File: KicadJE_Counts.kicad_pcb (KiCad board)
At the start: 2 copper layers, 242 x 128 mm, 214 parts, among them J101 In7, J102 In6, J103 In3, J104 Out10, J105 Out11, J106 Out9, J107 Out6, J201 ClockOut, J202 ClockIn, J203 Out0, J204 Out1, J205 Out2, J206 Out3, J207 Out4, J208 Out5, J209 Out6, J210 Out7, J211 Out8, J212 Out9, J213 Reset, J214 Hold, J301 Doepfer connector, J302 In_1, J303 In 2, J304 Out 1, J305 Out 2, J306 Out 1 Final, J307 Out 2 Final, P201 HEADER_2x5_Doepfer, SW201 Run, U201 LM555, U202 4017, U301 TL072, U302 TL072

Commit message: Update KicadJE_Counts.kicad_pcb
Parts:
- moved RV301 111.4 mm to (52.5, 67.5)
- moved RV303 103.2 mm to (87.5, 62.5), turned to 180 degrees
- moved RV304 102.3 mm to (87.5, 82.5), turned to 180 degrees
- moved RV302 75.9 mm to (52.8, 87.5)
- moved J303 70.4 mm to (80.0, 115.0), turned to 90 degrees
- moved D311 54.1 mm to (86.5, 145.0), turned to 270 degrees
- moved C312 51.7 mm to (86.7, 173.8)
- moved R306 51.7 mm to (91.4, 174.2)
- moved R314 51.7 mm to (97.2, 174.6)
- moved D302 51.7 mm to (90.4, 236.3)
- moved D309 51.7 mm to (90.7, 239.6)
- moved J304 51.5 mm to (60.0, 135.0), turned to 270 degrees
- moved J302 51.5 mm to (60.0, 115.0), turned to 270 degrees
- moved C311 50.7 mm to (92.2, 178.2)
- moved C322 50.7 mm to (87.4, 178.2)
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
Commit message: Update KicadJE_Counts.kicad_pcb
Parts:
- added D317: LED, AJ:LED_0805_2012Metric_Pad1.15x1.40mm_HandSolder, F.Cu at (69.9, 51.0)
- added R334: 10k, AJ:R_0805_AJ, F.Cu at (65.5, 51.0)
- moved J301 0.50 mm to (68.8, 53.2)
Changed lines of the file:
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@@
     (tracks 486)
     (zones 0)
-    (modules 214)
-    (nets 101)
+    (modules 216)
+    (nets 102)
   )
   (page A4)
@@
   (net 99 /KicadJE_Counts2/POT3_H)
   (net 100 /KicadJE_Counts2/POT4_H)
+  (net 101 "Net-(D317-Pad1)")
   (net_class Default "This is the default net class."
     (clearance 0.15)
@@
     (add_net "Net-(D311-Pad2)")
     (add_net "Net-(D312-Pad2)")
+    (add_net "Net-(D317-Pad1)")
     (add_net "Net-(J101-PadT)")
     (add_net "Net-(J102-PadT)")
@@
   )
   (module Connector_PinSocket_2.54mm:PinSocket_2x08_P2.54mm_Vertical (layer B.Cu)
-    (at 68.71 52.75 180)
+    (at 68.75 53.25 180)
     (descr "Through hole straight socket strip, 2x08, 2.54mm pitch, double cols (from Kicad 4.0.7), script generated")
     (tags "Through hole socket strip THT 2x08 2.54mm double row")
@@
       (at (xyz 0 0 0))
       (scale (xyz 1 1 1))
+      (rotate (xyz 0 0 0))
+    )
+  )
+  (module AJ:LED_0805_2012Metric_Pad1.15x1.40mm_HandSolder (layer F.Cu)
+    (at 69.920001 51.020001)
+    (descr "LED SMD 0805 (2012 Metric), square (rectangular) end terminal, IPC_7351 nominal, (Body size source: https://docs.google.com/spreadsheets/d/1BsfQQcO9C6DZCsRaXUlFlo91Tg2WpOkGARC1WS5S8t0/edit?usp=sharing), generated with kicad-footprint-generator")
+    (tags "LED handsolder")
+    (attr smd)
+    (fp_text reference D317 (at 4.079999 -0.020001) (layer F.SilkS)
+      (effects (font (size 1 1) (thickness 0.15)))
+    )
+    (fp_text value LED (at 4.829999 1.479999) (layer F.SilkS)
+      (effects (font (size 1 1) (thickness 0.1)))
+    )
+    (fp_text user %R (at 0 0) (layer F.Fab)
+      (effects (font (size 0.5 0.5) (thickness 0.08)))
+    )
+    (fp_line (start 1.85 0.95) (end -1.85 0.95) (layer F.CrtYd) (width 0.05))
+    (fp_line (start 1.85 -0.95) (end 1.85 0.95) (layer F.CrtYd) (width 0.05))
+    (fp_line (start -1.85 -0.95) (end 1.85 -0.95) (layer F.CrtYd) (width 0.05))
+    (fp_line (start -1.85 0.95) (end -1.85 -0.95) (layer F.CrtYd) (width 0.05))
+    (fp_line (start -1.86 0.96) (end 1 0.96) (layer F.SilkS) (width 0.12))
+    (fp_line (start -1.86 -0.96) (end -1.86 0.96) (layer F.SilkS) (width 0.12))
+    (fp_line (start 1 -0.96) (end -1.86 -0.96) (layer F.SilkS) (width 0.12))
+    (fp_line (start 1 0.6) (end 1 -0.6) (layer F.Fab) (width 0.1))
+    (fp_line (start -1 0.6) (end 1 0.6) (layer F.Fab) (width 0.1))
+    (fp_line (start -1 -0.3) (end -1 0.6) (layer F.Fab) (width 0.1))
+    (fp_line (start -0.7 -0.6) (end -1 -0.3) (layer F.Fab) (width 0.1))
+    (fp_line (start 1 -0.6) (end -0.7 -0.6) (layer F.Fab) (width 0.1))
+    (pad 2 smd roundrect (at 1.025 0) (size 1.15 1.4) (layers F.Cu F.Paste F.Mask) (roundrect_rratio 0.217391)
+      (net 1 GND))
+    (pad 1 smd roundrect (at -1.025 0) (size 1.15 1.4) (layers F.Cu F.Paste F.Mask) (roundrect_rratio 0.217391)
+      (net 101 "Net-(D317-Pad1)"))
+    (model ${KISYS3DMOD}/LED_SMD.3dshapes/LED_0805_2012Metric.wrl
+      (at (xyz 0 0 0))
+      (scale (xyz 1 1 1))
+      (rotate (xyz 0 0 0))
+    )
+  )
+  (module AJ:R_0805_AJ (layer F.Cu)
+    (at 65.5 51)
+    (descr "Resistor SMD 0805 (2012 Metric), square (rectangular) end terminal, IPC_7351 nominal with elongated pad for handsoldering. (Body size source: https://docs.google.com/spreadsheets/d/1BsfQQcO9C6DZCsRaXUlFlo91Tg2WpOkGARC1WS5S8t0/edit?usp=sharing), generated with kicad-footprint-generator")
+    (tags "resistor handsolder")
+    (attr smd)
+    (fp_text reference R334 (at -4 0.024999) (layer F.SilkS)
+      (effects (font (size 1 1) (thickness 0.15)))
+    )
+    (fp_text value 10k (at 0 1.65) (layer F.SilkS)
+      (effects (font (size 0.8 0.8) (thickness 0.1)))
+    )
+    (fp_line (start -1 0.6) (end -1 -0.6) (layer F.Fab) (width 0.1))
+    (fp_line (start -1 -0.6) (end 1 -0.6) (layer F.Fab) (width 0.1))
+    (fp_line (start 1 -0.6) (end 1 0.6) (layer F.Fab) (width 0.1))
+    (fp_line (start 1 0.6) (end -1 0.6) (layer F.Fab) (width 0.1))
+    (fp_line (start -0.261252 -0.71) (end 0.261252 -0.71) (layer F.SilkS) (width 0.12))
+    (fp_line (start -0.261252 0.71) (end 0.261252 0.71) (layer F.SilkS) (width 0.12))
+    (fp_line (start -1.85 0.95) (end -1.85 -0.95) (layer F.CrtYd) (width 0.05))
+    (fp_line (start -1.85 -0.95) (end 1.85 -0.95) (layer F.CrtYd) (width 0.05))
+    (fp_line (start 1.85 -0.95) (end 1.85 0.95) (layer F.CrtYd) (width 0.05))
+    (fp_line (start 1.85 0.95) (end -1.85 0.95) (layer F.CrtYd) (width 0.05))
+    (fp_text user %R (at 0 0) (layer F.Fab)
+      (effects (font (size 0.5 0.5) (thickness 0.08)))
+    )
+    (pad 1 smd roundrect (at -1.025 0) (size 1.15 1.4) (layers F.Cu F.Paste F.Mask) (roundrect_rratio 0.217391)
+      (net 18 -12V))
+    (pad 2 smd roundrect (at 1.025 0) (size 1.15 1.4) (layers F.Cu F.Paste F.Mask) (roundrect_rratio 0.217391)
+      (net 101 "Net-(D317-Pad1)"))
+    (model ${KISYS3DMOD}/Resistor_SMD.3dshapes/R_0805_2012Metric.wrl
+      (at (xyz 0 0 0))
+      (scale (xyz 1 1 1))

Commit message: Update KicadJE_Counts.kicad_pcb
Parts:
- C305, C306: moved to F.Cu
- RV301: value 100k_A4 -> 100k_1.1
- RV302: value 100k_A4 -> 100k_1.2
- RV303: value 100k_A4 -> 100k_2.1
- RV304: value 100k_A4 -> 100k_2.2
- moved C305 160.6 mm to (74.0, 56.4), turned to 90 degrees
- moved C306 155.3 mm to (65.8, 56.2), turned to 270 degrees
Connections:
- R328 pad 1: (no net) -> /KicadJE_Counts2/POT2_C
- RV301 pad 1: (no net) -> /KicadJE_Counts2/POT1_L
- RV301 pad 2: /KicadJE_Counts2/POT3_C -> /KicadJE_Counts2/POT1_C
- RV301 pad 3: /KicadJE_Counts2/POT3_H -> (no net)
- RV302 pad 1: /KicadJE_Counts2/POT4_L -> /KicadJE_Counts2/POT2_L
- RV302 pad 2: /KicadJE_Counts2/POT4_C -> /KicadJE_Counts2/POT2_C
- RV302 pad 3: /KicadJE_Counts2/POT4_H -> (no net)
- RV303 pad 3: /KicadJE_Counts2/POT3_H -> (no net)
- RV304 pad 3: /KicadJE_Counts2/POT4_H -> (no net)

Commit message: Update KicadJE_Counts.kicad_pcb
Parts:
- added H301: ON, AJ:LED_Hole_3mm, F.Cu at (102.0, 52.0)
- added TP301: In1, AJ:Jack_6m3, F.Cu at (102.0, 115.0)
- added TP302: Tri, AJ:Jack_6m3, F.Cu at (102.0, 135.0)
- added TP303: SQ, AJ:Jack_6m3, F.Cu at (102.0, 145.0)
- added TP304: PWM1, AJ:Pot_6m3_scale1, F.Cu at (102.0, 65.0)
- added TP305: PWM2, AJ:Pot_6m3_scale1, F.Cu at (102.0, 85.0)
- D301, D302: moved to F.Cu
- moved D302 182.8 mm to (60.0, 56.0), turned to 270 degrees
- moved D301 164.5 mm to (80.0, 56.0), turned to 90 degrees
- moved U302 130.0 mm to (60.0, 100.0), turned to 180 degrees
- moved U301 125.4 mm to (80.0, 100.0), turned to 180 degrees
- moved C309 103.4 mm to (60.0, 96.0), turned to 180 degrees
- moved C314 100.9 mm to (72.0, 115.0), turned to 180 degrees
- moved C310 100.4 mm to (60.0, 105.0)
- moved C313 97.3 mm to (68.0, 115.0)
- moved C311 83.1 mm to (80.0, 96.0), turned to 180 degrees
- moved D304 77.1 mm to (129.4, 192.7)
- moved D309 77.1 mm to (133.7, 175.6)
- moved D306 77.1 mm to (129.8, 187.5)
- moved D307 77.1 mm to (119.8, 186.5)
- moved D308 77.1 mm to (119.7, 175.4)
- moved D310 77.1 mm to (119.7, 172.1)
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
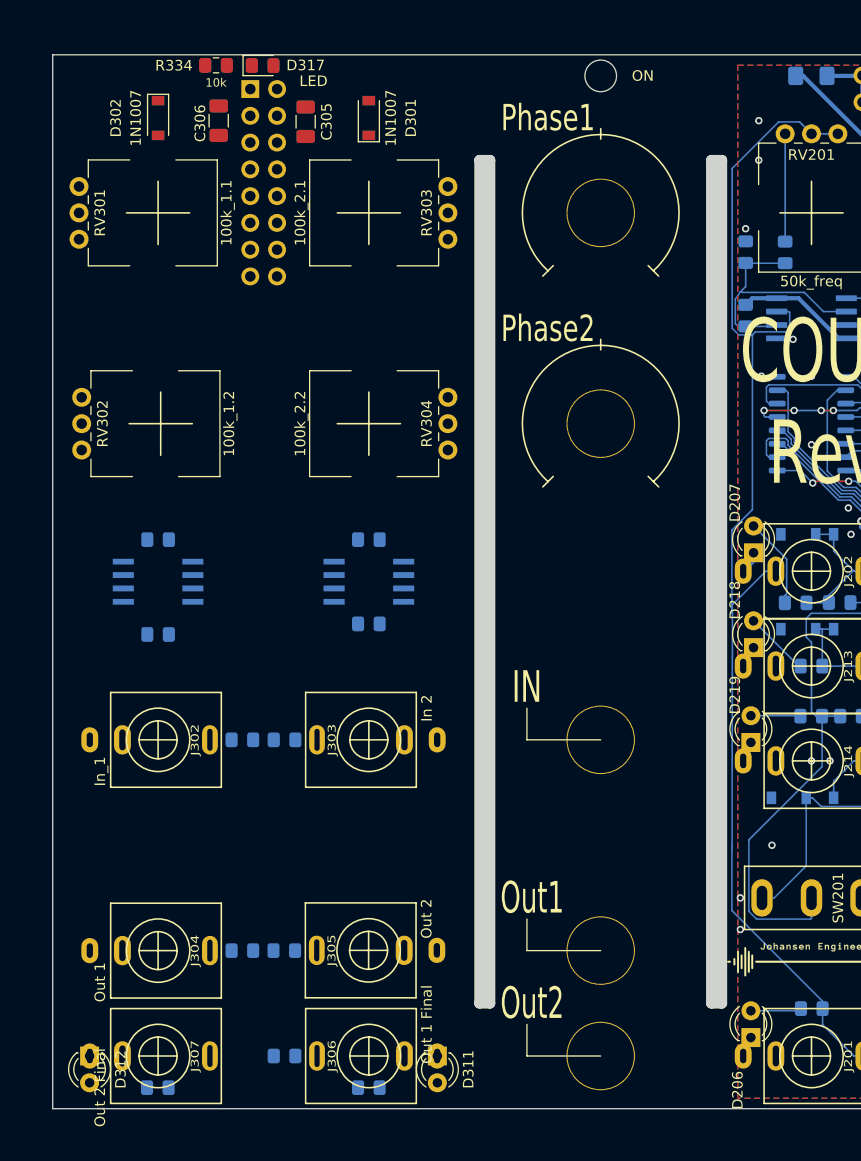
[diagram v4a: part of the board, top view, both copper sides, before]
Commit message: Update KicadJE_Counts.kicad_pcb
LED and GND on center panel
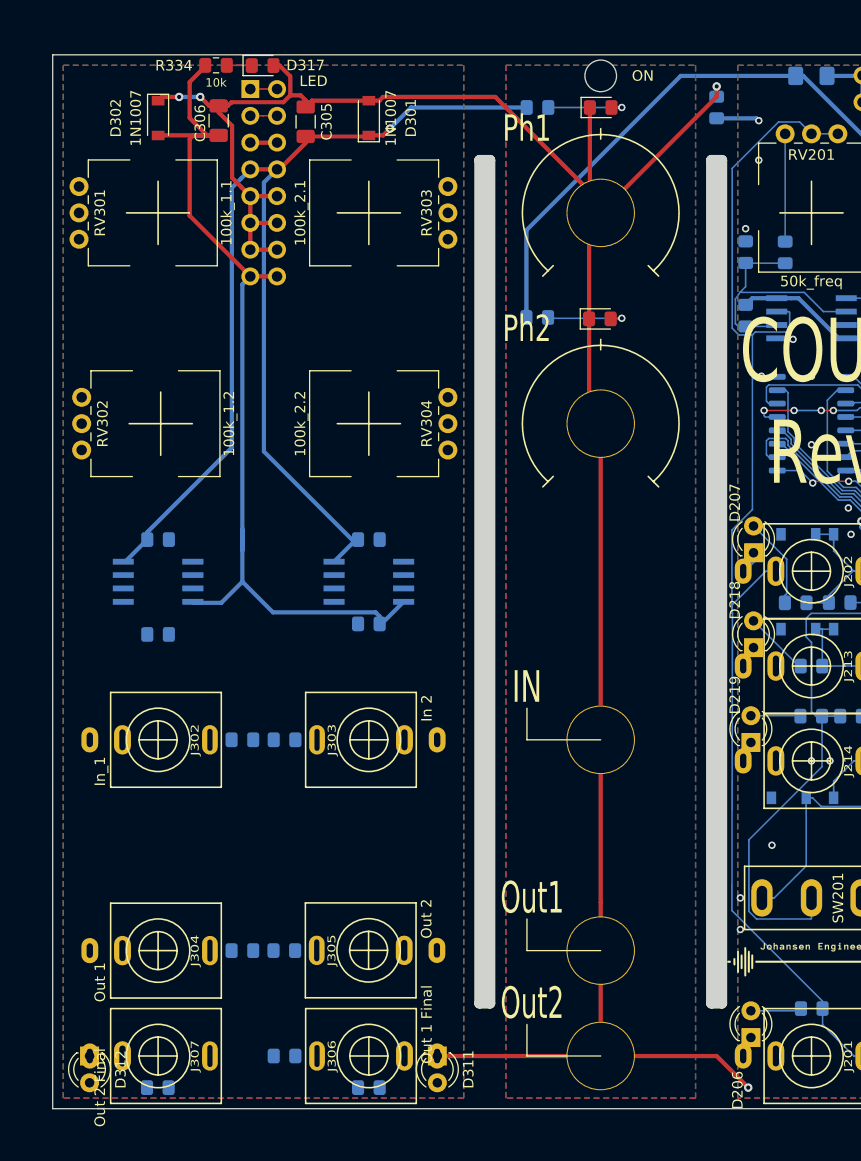
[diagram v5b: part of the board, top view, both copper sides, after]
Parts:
- added D101: D_LED, AJ:LED_0805_2012Metric_Pad1.15x1.40mm_HandSolder, F.Cu at (102.0, 55.0)
- added D102: D_LED, AJ:LED_0805_2012Metric_Pad1.15x1.40mm_HandSolder, F.Cu at (101.9, 75.1)
- added R107: DNP, AJ:R_0805_AJ, B.Cu at (96.0, 55.0)
- added R108: DNP, AJ:R_0805_AJ, B.Cu at (96.0, 74.9)
- added R109: DNP, AJ:R_0805_AJ, B.Cu at (113.0, 55.0)
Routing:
- net GND: track 0.00 -> 215.2 mm, vias 0 -> 4
- net +12V: track 0.00 -> 114.2 mm, vias 0 -> 1
- net -12V: track 0.00 -> 90.7 mm
- net +12Vc: track 94.1 -> 133.9 mm
- net Net-(D102-Pad2): track 0.00 -> 8.11 mm, vias 0 -> 1
- net Net-(D101-Pad2): track 0.00 -> 7.95 mm, vias 0 -> 1
- net GNDS: track 59.6 -> 63.7 mm
- net /KicadJE_Counts2/Gate: track 0.00 -> 2.54 mm
- net /KicadJE_Counts2/CV: track 0.00 -> 2.54 mm
- net +5V: track 0.00 -> 2.54 mm
- net Net-(D317-Pad1): track 0.00 -> 2.38 mm
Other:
- board text added: "Ph1"
- board text added: "Ph2"

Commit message: Update KicadJE_Counts.kicad_pcb
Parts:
- moved R109 3.00 mm to (110.0, 55.0)
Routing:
- net GND: track 215.2 -> 198.7 mm
- net GNDS: track 63.7 -> 66.7 mm
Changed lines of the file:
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@@
     (thickness 1.6)
     (drawings 219)
-    (tracks 607)
+    (tracks 606)
     (zones 0)
     (modules 227)
@@
   )
   (module AJ:R_0805_AJ (layer B.Cu)
-    (at 113 55 90)
+    (at 110 55 90)
     (descr "Resistor SMD 0805 (2012 Metric), square (rectangular) end terminal, IPC_7351 nominal with elongated pad for handsoldering. (Body size source: https://docs.google.com/spreadsheets/d/1BsfQQcO9C6DZCsRaXUlFlo91Tg2WpOkGARC1WS5S8t0/edit?usp=sharing), generated with kicad-footprint-generator")
     (tags "resistor handsolder")
@@
   (segment (start 80 54.35) (end 81 54.35) (width 0.4) (layer F.Cu) (net 1) (status 10))
   (segment (start 81 54.35) (end 81.35 54) (width 0.4) (layer F.Cu) (net 1))
-  (segment (start 113 54) (end 113 53) (width 0.4) (layer F.Cu) (net 1))
-  (via (at 113 53) (size 0.8) (drill 0.4) (layers F.Cu B.Cu) (net 1))
-  (segment (start 102 65) (end 113 54) (width 0.4) (layer F.Cu) (net 1))
-  (segment (start 113 53) (end 113 53.975) (width 0.4) (layer B.Cu) (net 1))
+  (via (at 110 53) (size 0.8) (drill 0.4) (layers F.Cu B.Cu) (net 1))
+  (segment (start 110 54) (end 110 53) (width 0.4) (layer B.Cu) (net 1))
   (segment (start 120.79 140.71) (end 121 140.5) (width 0.15) (layer B.Cu) (net 5) (status 30))
   (segment (start 116.25 140.71) (end 120.79 140.71) (width 0.15) (layer B.Cu) (net 5) (status 30))
@@
   (segment (start 118.7 76.905) (end 120.155 76.905) (width 0.4) (layer B.Cu) (net 12) (status 10))
   (segment (start 116.775 56.025) (end 117 56.25) (width 0.4) (layer B.Cu) (net 12))
-  (segment (start 113 56.025) (end 116.775 56.025) (width 0.4) (layer B.Cu) (net 12))
+  (segment (start 110 56) (end 110.025 56.025) (width 0.4) (layer B.Cu) (net 12))
+  (segment (start 110.025 56.025) (end 116.775 56.025) (width 0.4) (layer B.Cu) (net 12))
   (segment (start 115.75 75.775) (end 118.56 75.775) (width 0.15) (layer B.Cu) (net 13) (status 30))
   (segment (start 114.77499 75.49999) (end 115.05 75.775) (width 0.15) (layer B.Cu) (net 13) (status 20))

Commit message: Update KicadJE_Counts.kicad_pcb
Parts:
- added J108: Conn_02x03_Male, Connector_PinHeader_2.54mm:PinHeader_2x03_P2.54mm_Vertical_SMD, B.Cu at (102.0, 58.0)
- moved R109 2.00 mm to (108.0, 55.0), turned to 270 degrees
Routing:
- net GNDS: track 66.7 -> 87.9 mm
- net +12V: track 114.2 -> 125.4 mm
- net +12Vc: track 133.9 -> 136.4 mm
- net GND: track 198.7 -> 197.7 mm, vias 4 -> 3

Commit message: cleanup old conn
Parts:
- removed J101: In7, AJ-Dropbox-Kicad:PJ301SM
- removed J102: In6, AJ-Dropbox-Kicad:PJ301SM
- removed J103: In3, AJ-Dropbox-Kicad:PJ301SM
- removed J104: Out10, AJ-Dropbox-Kicad:PJ301SM
- removed J105: Out11, AJ-Dropbox-Kicad:PJ301SM
- removed J106: Out9, AJ-Dropbox-Kicad:PJ301SM
- removed J107: Out6, AJ-Dropbox-Kicad:PJ301SM
- removed R101, R102, R103, R104, R105, R106: 10k, AJ:R_0805_AJ
- moved D303 109.3 mm to (67.6, 109.5)
- moved D304 100.7 mm to (72.8, 109.5)
- moved D306 94.6 mm to (72.8, 112.0)
- moved D305 91.7 mm to (67.6, 112.0)
- moved R305 75.5 mm to (80.0, 115.0)
- moved D314 71.7 mm to (56.2, 155.2), turned to 180 degrees
- moved D313 65.6 mm to (56.4, 157.6)
- moved D307 61.3 mm to (65.8, 157.5), turned to 180 degrees
- moved D308 57.4 mm to (65.9, 155.4)
- moved D309 56.8 mm to (79.4, 158.8)
- moved H302 55.6 mm to (25.8, 196.0)
- moved H301 55.6 mm to (2.53, 183.5)
- moved H303 55.6 mm to (13.2, 199.0)
- moved D310 43.3 mm to (79.2, 156.5), turned to 180 degrees
- moved H304 42.9 mm to (19.5, 183.8)
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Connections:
- J108 pad 5: GNDS -> GND
- J108 pad 6: GNDS -> GND
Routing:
- net +12V: track 125.4 -> 141.7 mm
- net GNDS: track 87.9 -> 78.2 mm
- net +12Vc: track 136.4 -> 138.6 mm
- net GND: vias 3 -> 5
